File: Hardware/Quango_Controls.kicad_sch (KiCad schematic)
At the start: 32 parts, among them J1 Conn_01x12_Male, J2 Conn_01x12_Male, J3 Conn_01x12_Male, J4 Conn_01x12_Male, J5 CV_A, J6 CV_B, J7 Out, J8 USB_C_Receptacle, J9 Midi_In, SW1 SW_Push, SW2 SW_Push

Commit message: Reduced module size to 14HP; updated to Amphenol USB C
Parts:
- J8: footprint Connector_USB:USB_C_Receptacle_JAE_DX07S024WJ3R400 -> Custom_Footprints:USB_C_Receptacle_Amphenol_12401951E412A
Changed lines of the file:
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@@
     (property "Reference" "J8" (id 0) (at 243.84 19.05 0))
     (property "Value" "USB_C_Receptacle" (id 1) (at 243.84 21.59 0))
-    (property "Footprint" "Connector_USB:USB_C_Receptacle_JAE_DX07S024WJ3R400" (id 2) (at 247.65 52.07 0)
+    (property "Footprint" "Custom_Footprints:USB_C_Receptacle_Amphenol_12401951E412A" (id 2) (at 247.65 52.07 0)
       (effects (font (size 1.27 1.27)) hide)
     )
@@
     )
     (path "/06738ae6-6b99-4285-8a79-2cc6ab0044fc"
-      (reference "J8") (unit 1) (value "USB_C_Receptacle") (footprint "Connector_USB:USB_C_Receptacle_JAE_DX07S024WJ3R400")
+      (reference "J8") (unit 1) (value "USB_C_Receptacle") (footprint "Custom_Footprints:USB_C_Receptacle_Amphenol_12401951E412A")
     )
     (path "/50ae117b-ba18-40c9-8318-325af3127371"

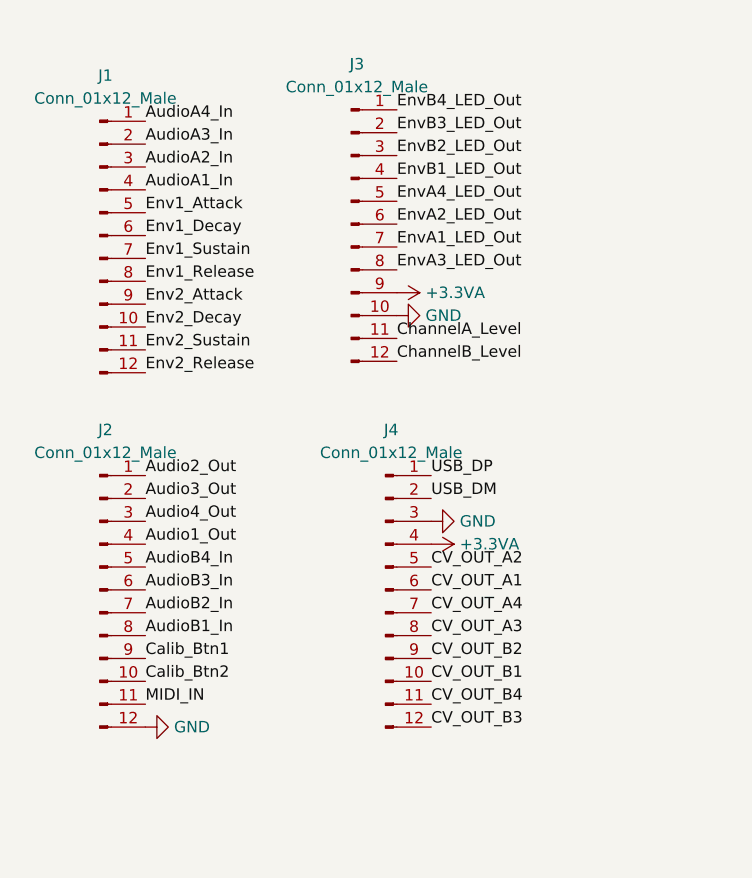
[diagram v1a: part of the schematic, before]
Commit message: First draft routing of control board
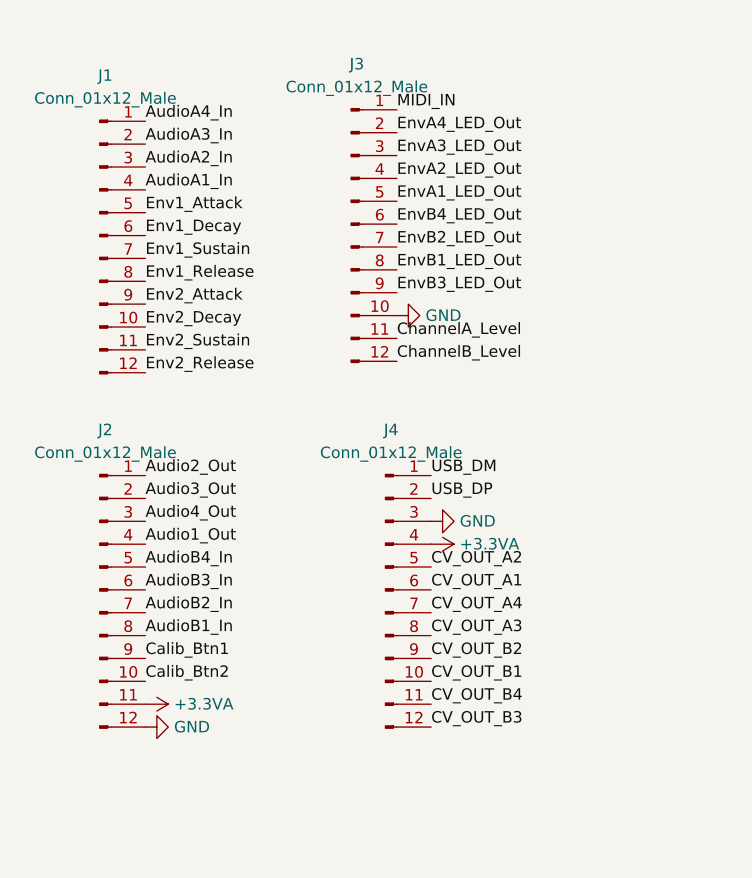
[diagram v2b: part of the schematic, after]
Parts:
- R1, R2: footprint Resistor_SMD:R_0201_0603Metric -> Resistor_SMD:R_0805_2012Metric
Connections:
- net +3.3VA: now also J2.11 (Pin_11); no longer J3.9 (Pin_9)
- net EnvA1_LED_Out: now also J3.5 (Pin_5); no longer J3.7 (Pin_7)
- net EnvA2_LED_Out: now also J3.4 (Pin_4); no longer J3.6 (Pin_6)
- net EnvA3_LED_Out: now also J3.3 (Pin_3); no longer J3.8 (Pin_8)
- net EnvA4_LED_Out: now also J3.2 (Pin_2); no longer J3.5 (Pin_5)
- net EnvB1_LED_Out: now also J3.8 (Pin_8); no longer J3.4 (Pin_4)
- net EnvB2_LED_Out: now also J3.7 (Pin_7); no longer J3.3 (Pin_3)
- net EnvB3_LED_Out: now also J3.9 (Pin_9); no longer J3.2 (Pin_2)
- net EnvB4_LED_Out: now also J3.6 (Pin_6); no longer J3.1 (Pin_1)
- net MIDI_IN: now also J3.1 (Pin_1); no longer J2.11 (Pin_11)
- net USB_DM: now also J4.1 (Pin_1); no longer J4.2 (Pin_2)
- net USB_DP: now also J4.2 (Pin_2); no longer J4.1 (Pin_1)

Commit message: Schematic Clean Up
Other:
- note added: "Buttons"
- note added: "Connectors"
- note added: "Envelope Potentiometers"
- note added: "LEDs"
- note added: "Level Slide Potentiometers"
- note added: "MIDI"
- note added: "RJ45"
- note added: "USB"
- moved on the sheet: A1, A2, A3, A4, B1, B2, B3, B4, Env1, Env2, Env3, Env4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

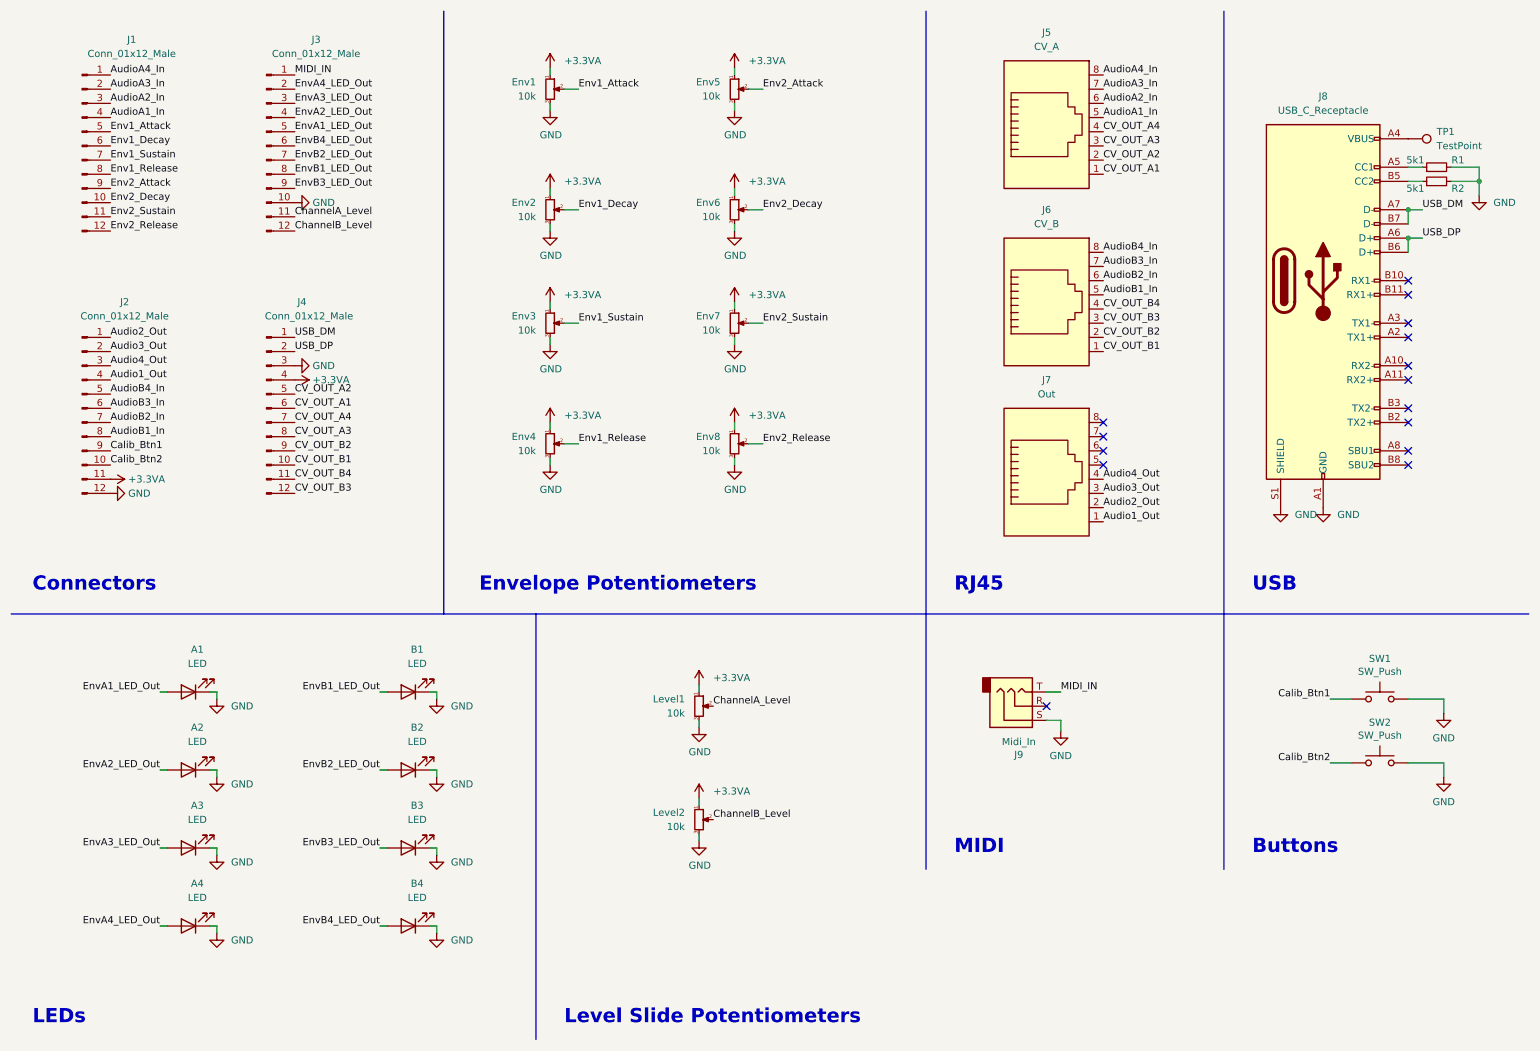
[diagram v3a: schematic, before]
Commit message: Increased size to 16HP
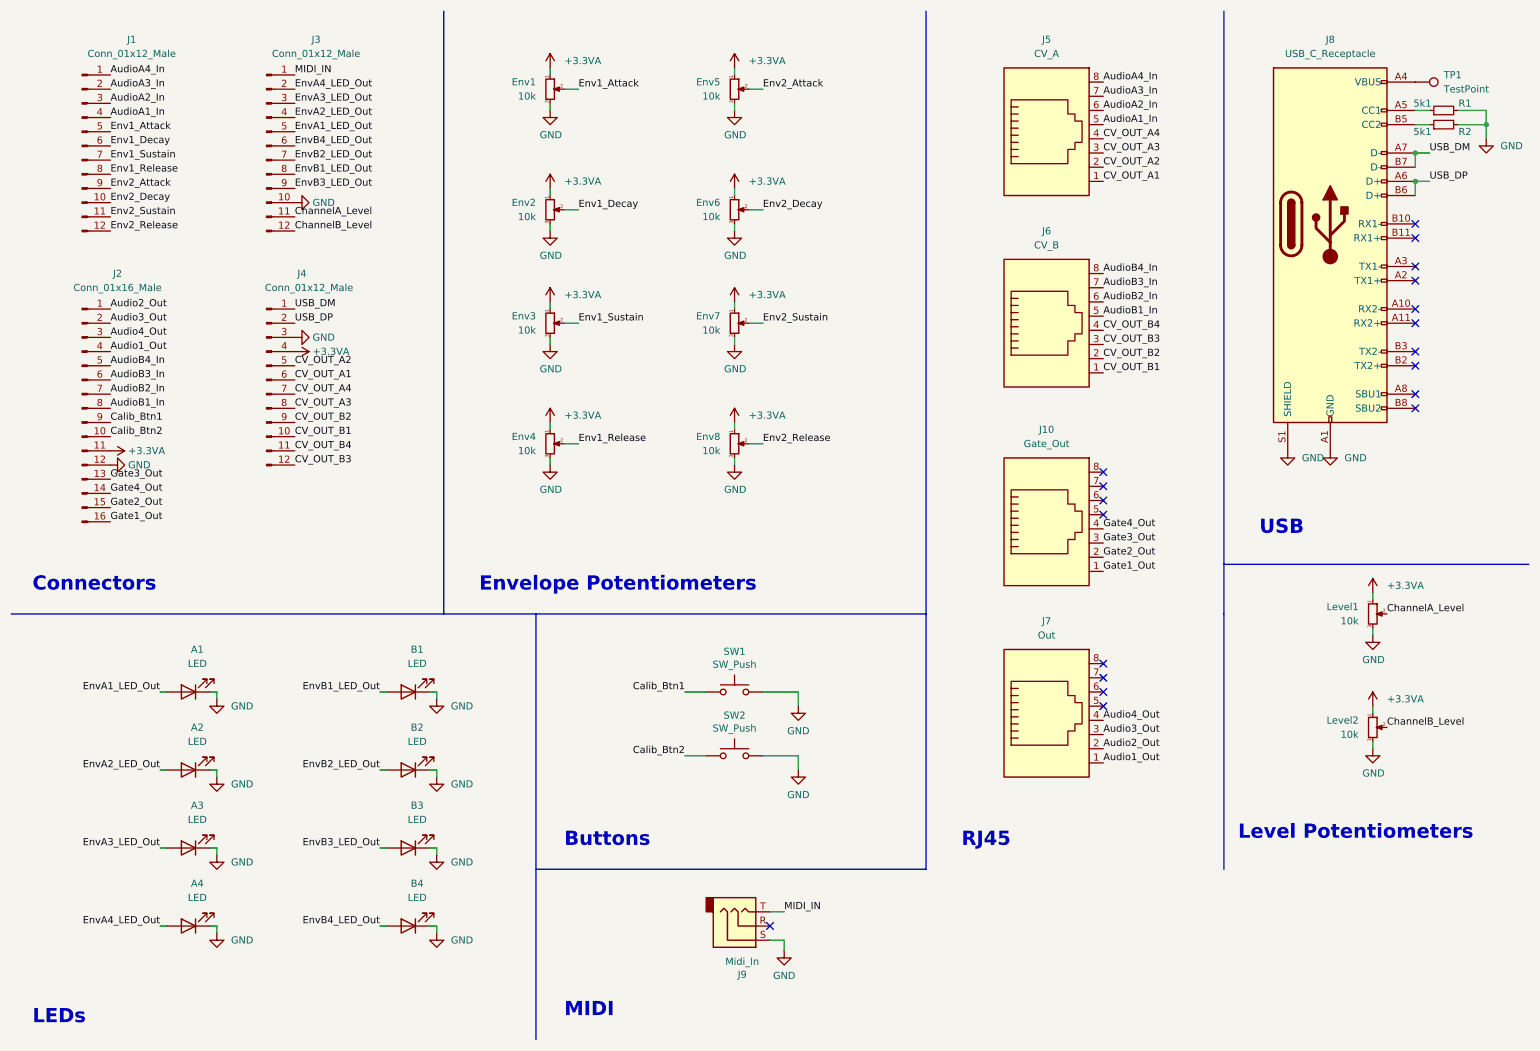
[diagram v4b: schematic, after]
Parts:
- removed J2: Conn_01x12_Male, Connector_PinHeader_2.54mm:PinHeader_1x12_P2.54mm_Vertical, symbol Connector:Conn_01x12_Male
- added J10: Gate_Out, Custom_Footprints:RJ45_Molex_42878-8506, symbol Connector:RJ45
- added J2: Conn_01x16_Male, Connector_PinHeader_2.54mm:PinHeader_1x16_P2.54mm_Vertical, symbol Connector:Conn_01x16_Male
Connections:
- net +3.3VA: now also J2.11 (Pin_11)
- net Audio1_Out: now also J2.4 (Pin_4)
- net Audio2_Out: now also J2.1 (Pin_1)
- net Audio3_Out: now also J2.2 (Pin_2)
- net Audio4_Out: now also J2.3 (Pin_3)
- net AudioB1_In: now also J2.8 (Pin_8)
- net AudioB2_In: now also J2.7 (Pin_7)
- net AudioB3_In: now also J2.6 (Pin_6)
- net AudioB4_In: now also J2.5 (Pin_5)
- net Calib_Btn1: now also J2.9 (Pin_9)
- net Calib_Btn2: now also J2.10 (Pin_10)
- net GND: now also J2.12 (Pin_12)
- new net Gate1_Out: J10.1, J2.16 (Pin_16)
- new net Gate2_Out: J10.2, J2.15 (Pin_15)
- new net Gate3_Out: J10.3, J2.13 (Pin_13)
- new net Gate4_Out: J10.4, J2.14 (Pin_14)
- no-connect marks 15 -> 19
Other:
- note added: "Level Potentiometers"
- note removed: "Level Slide Potentiometers"
- moved on the sheet: J4, J5, J6, J7, J8, J9, Level1, Level2, R1, R2, SW1, SW2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

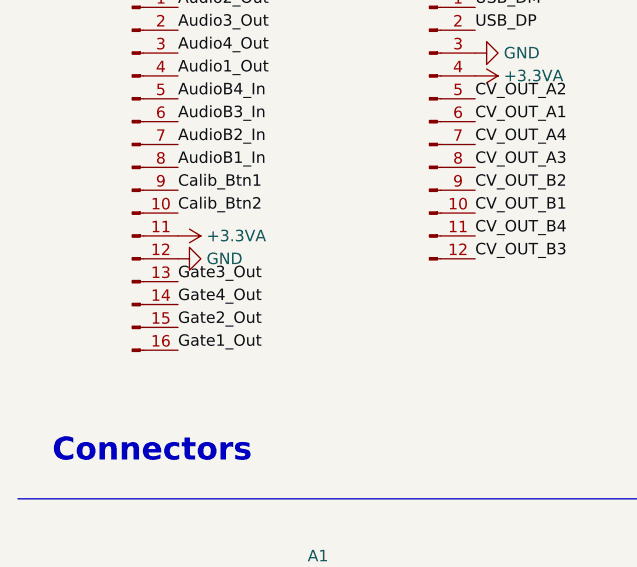
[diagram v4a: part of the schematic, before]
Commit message: Added breakout for gates on component board
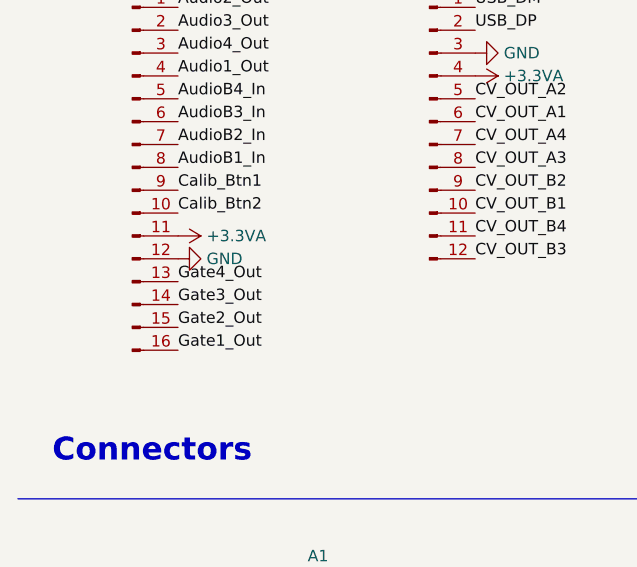
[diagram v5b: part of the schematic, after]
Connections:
- net Gate3_Out: now also J2.14 (Pin_14); no longer J2.13 (Pin_13)
- net Gate4_Out: now also J2.13 (Pin_13); no longer J2.14 (Pin_14)
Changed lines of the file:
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@@
     (effects (font (size 1.27 1.27)) (justify left bottom))
   )
-  (label "Gate3_Out" (at 30.48 96.52 0)
+  (label "Gate3_Out" (at 30.48 99.06 0)
     (effects (font (size 1.27 1.27)) (justify left bottom))
   )
@@
     (effects (font (size 1.27 1.27)) (justify right bottom))
   )
-  (label "Gate4_Out" (at 30.48 99.06 0)
+  (label "Gate4_Out" (at 30.48 96.52 0)
     (effects (font (size 1.27 1.27)) (justify left bottom))
   )

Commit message: Final Updates for v1.0 production
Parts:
- J1, J3, J4: footprint Connector_PinHeader_2.54mm:PinHeader_1x12_P2.54mm_Vertical -> Connector_PinSocket_2.54mm:PinSocket_1x12_P2.54mm_Vertical
- J2: footprint Connector_PinHeader_2.54mm:PinHeader_1x16_P2.54mm_Vertical -> Connector_PinSocket_2.54mm:PinSocket_1x16_P2.54mm_Vertical
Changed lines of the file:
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@@
     (property "Reference" "J2" (id 0) (at 31.75 59.69 0))
     (property "Value" "Conn_01x16_Male" (id 1) (at 31.75 62.23 0))
-    (property "Footprint" "Connector_PinHeader_2.54mm:PinHeader_1x16_P2.54mm_Vertical" (id 2) (at 25.4 83.82 0)
+    (property "Footprint" "Connector_PinSocket_2.54mm:PinSocket_1x16_P2.54mm_Vertical" (id 2) (at 25.4 83.82 0)
       (effects (font (size 1.27 1.27)) hide)
     )
@@
     (property "Reference" "J3" (id 0) (at 67.31 17.78 0))
     (property "Value" "Conn_01x12_Male" (id 1) (at 67.31 20.32 0))
-    (property "Footprint" "Connector_PinHeader_2.54mm:PinHeader_1x12_P2.54mm_Vertical" (id 2) (at 58.42 36.83 0)
+    (property "Footprint" "Connector_PinSocket_2.54mm:PinSocket_1x12_P2.54mm_Vertical" (id 2) (at 58.42 36.83 0)
       (effects (font (size 1.27 1.27)) hide)
     )
@@
     (property "Reference" "J1" (id 0) (at 34.29 17.78 0))
     (property "Value" "Conn_01x12_Male" (id 1) (at 34.29 20.32 0))
-    (property "Footprint" "Connector_PinHeader_2.54mm:PinHeader_1x12_P2.54mm_Vertical" (id 2) (at 25.4 36.83 0)
+    (property "Footprint" "Connector_PinSocket_2.54mm:PinSocket_1x12_P2.54mm_Vertical" (id 2) (at 25.4 36.83 0)
       (effects (font (size 1.27 1.27)) hide)
     )
@@
     (property "Reference" "J4" (id 0) (at 64.77 59.69 0))
     (property "Value" "Conn_01x12_Male" (id 1) (at 66.04 62.23 0))
-    (property "Footprint" "Connector_PinHeader_2.54mm:PinHeader_1x12_P2.54mm_Vertical" (id 2) (at 58.42 78.74 0)
+    (property "Footprint" "Connector_PinSocket_2.54mm:PinSocket_1x12_P2.54mm_Vertical" (id 2) (at 58.42 78.74 0)
       (effects (font (size 1.27 1.27)) hide)
     )
@@
     )
     (path "/18f561e6-9d74-485f-8fa5-b63bbdab6142"
-      (reference "J1") (unit 1) (value "Conn_01x12_Male") (footprint "Connector_PinHeader_2.54mm:PinHeader_1x12_P2.54mm_Vertical")
+      (reference "J1") (unit 1) (value "Conn_01x12_Male") (footprint "Connector_PinSocket_2.54mm:PinSocket_1x12_P2.54mm_Vertical")
     )
     (path "/1311fb50-2165-4359-9353-a049f8eb599b"
-      (reference "J2") (unit 1) (value "Conn_01x16_Male") (footprint "Connector_PinHeader_2.54mm:PinHeader_1x16_P2.54mm_Vertical")
+      (reference "J2") (unit 1) (value "Conn_01x16_Male") (footprint "Connector_PinSocket_2.54mm:PinSocket_1x16_P2.54mm_Vertical")
     )
     (path "/166ffdad-7711-4b9b-a599-343161ca802e"
-      (reference "J3") (unit 1) (value "Conn_01x12_Male") (footprint "Connector_PinHeader_2.54mm:PinHeader_1x12_P2.54mm_Vertical")
+      (reference "J3") (unit 1) (value "Conn_01x12_Male") (footprint "Connector_PinSocket_2.54mm:PinSocket_1x12_P2.54mm_Vertical")
     )
     (path "/a6fa07da-6db2-4c5e-909a-1f8e0f888984"
-      (reference "J4") (unit 1) (value "Conn_01x12_Male") (footprint "Connector_PinHeader_2.54mm:PinHeader_1x12_P2.54mm_Vertical")
+      (reference "J4") (unit 1) (value "Conn_01x12_Male") (footprint "Connector_PinSocket_2.54mm:PinSocket_1x12_P2.54mm_Vertical")
     )
     (path "/fc9c2ee5-2d45-4c01-b1e9-147af3aa0586"
